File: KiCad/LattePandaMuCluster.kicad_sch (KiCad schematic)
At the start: 0 parts

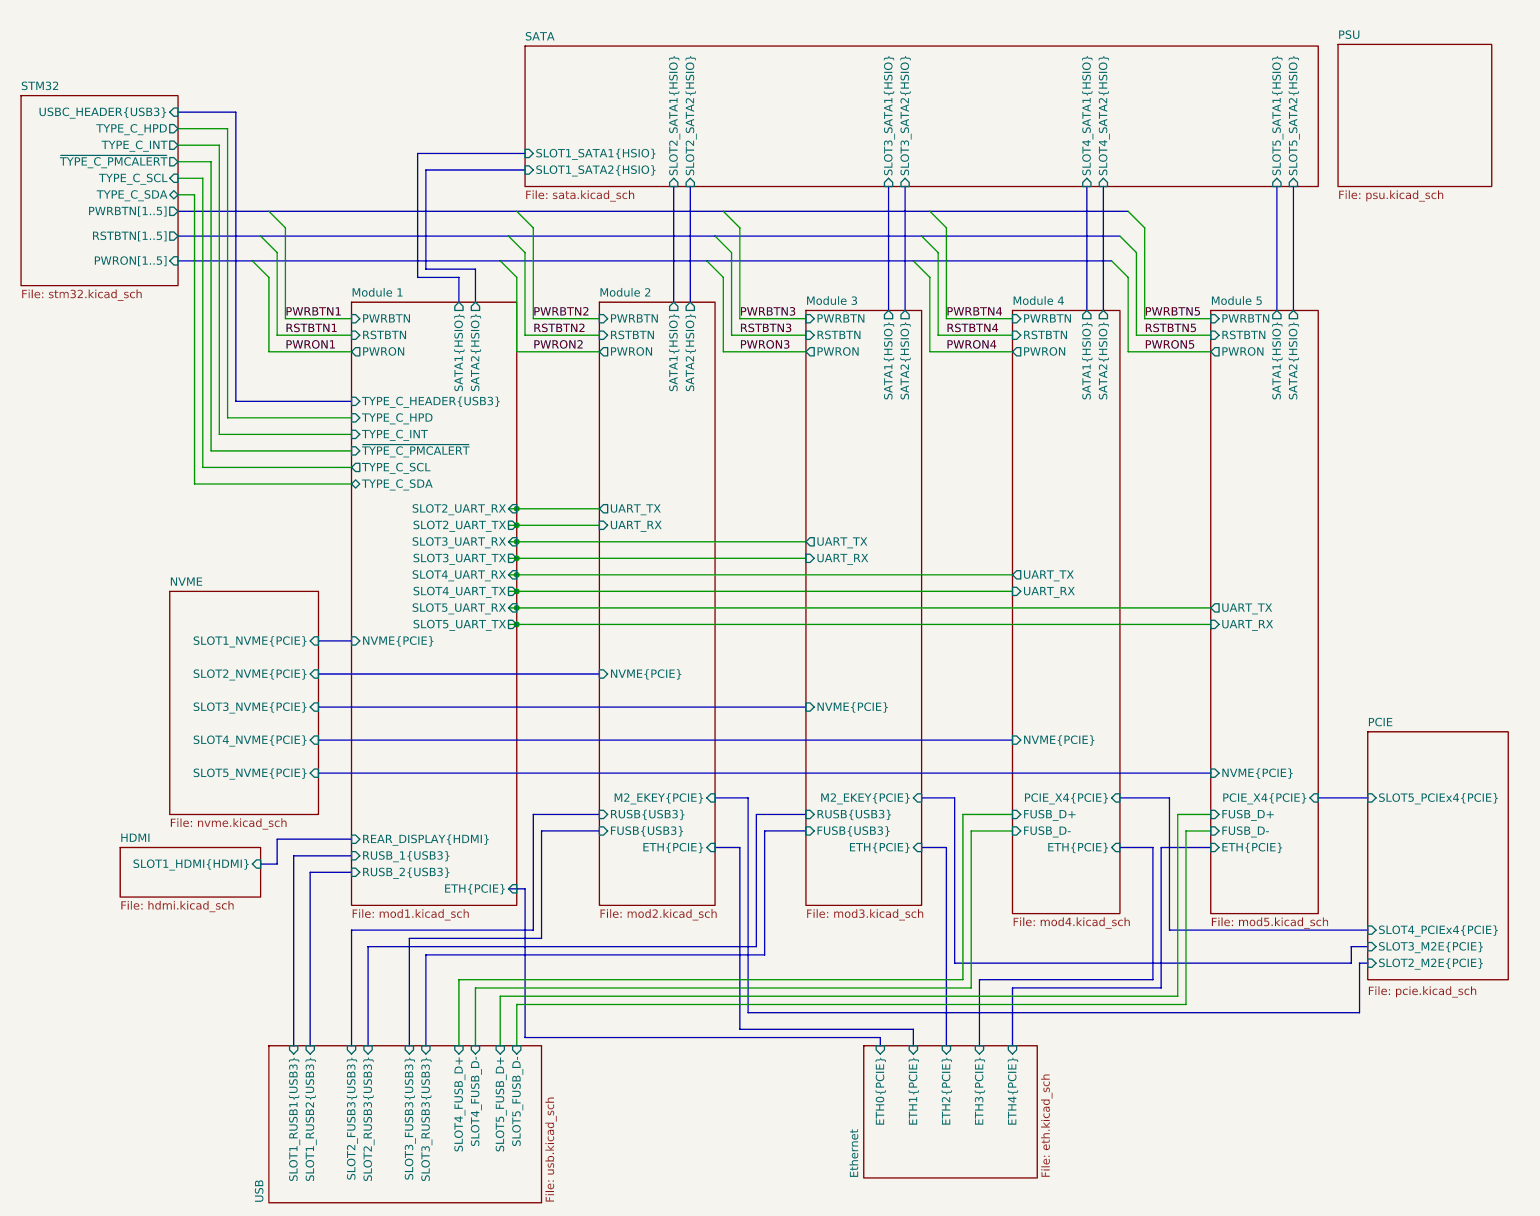
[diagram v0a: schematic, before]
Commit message: Add programming header and power and reset switches
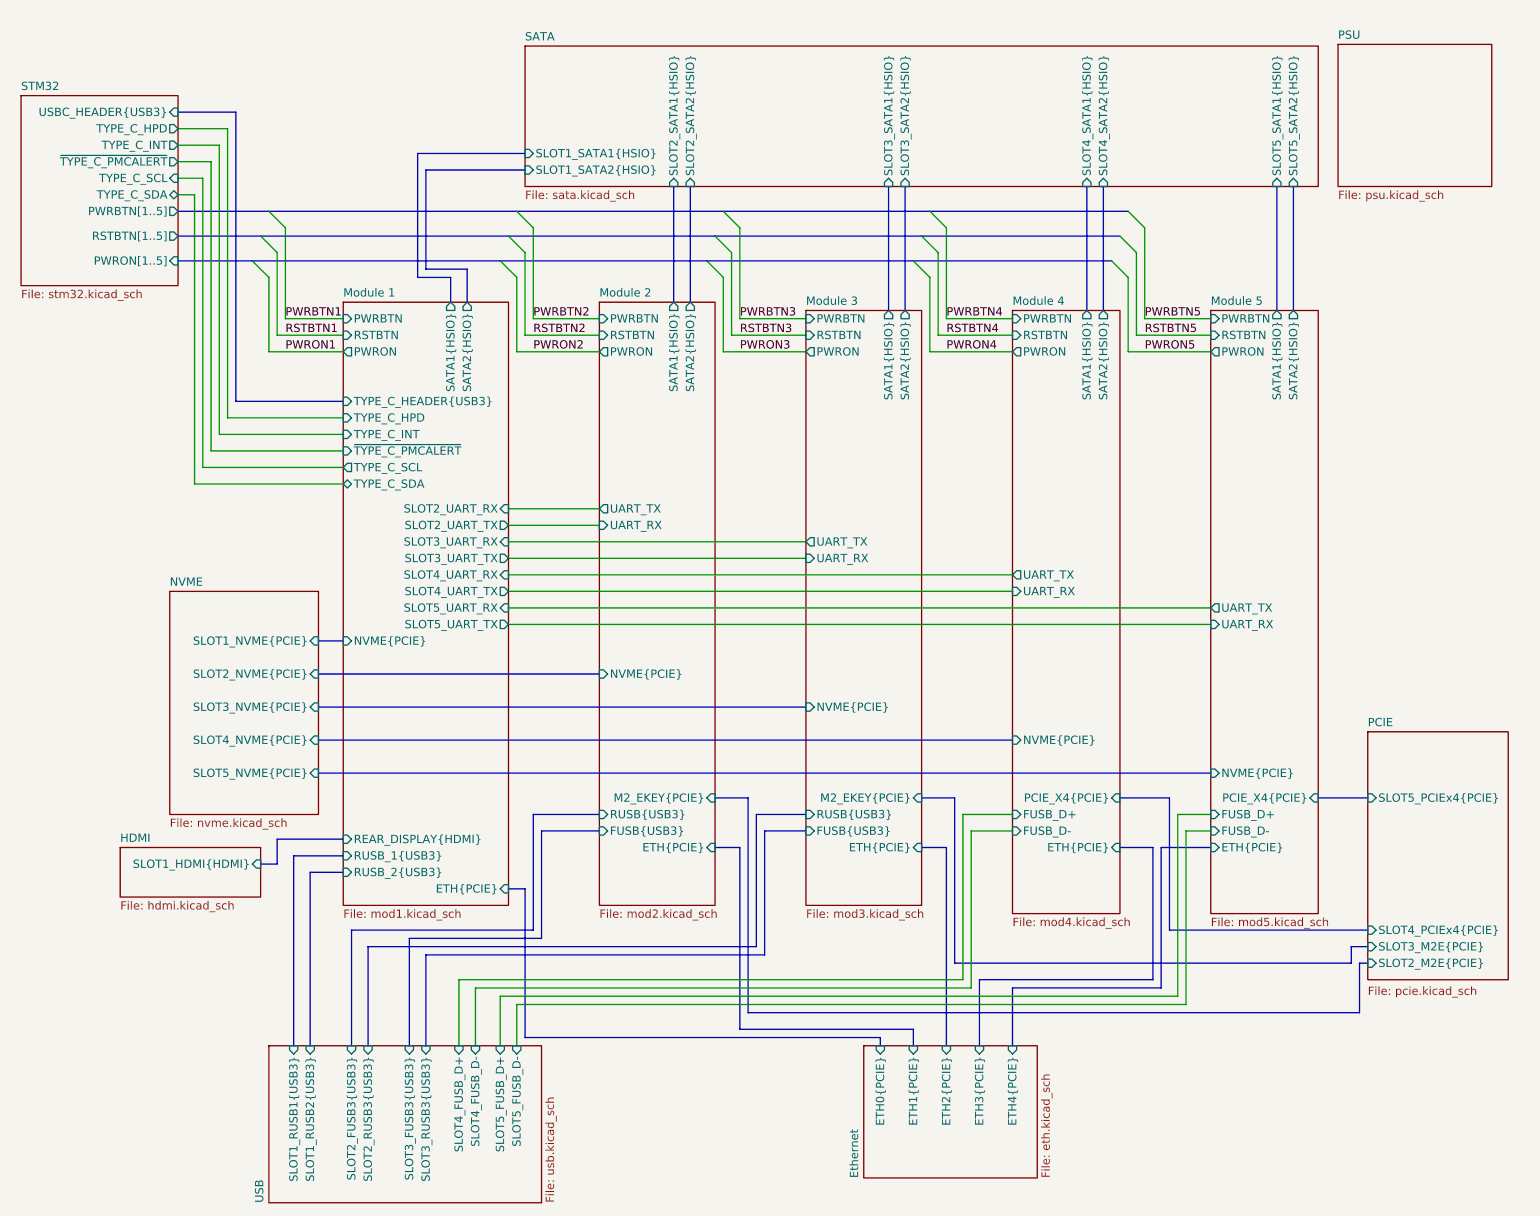
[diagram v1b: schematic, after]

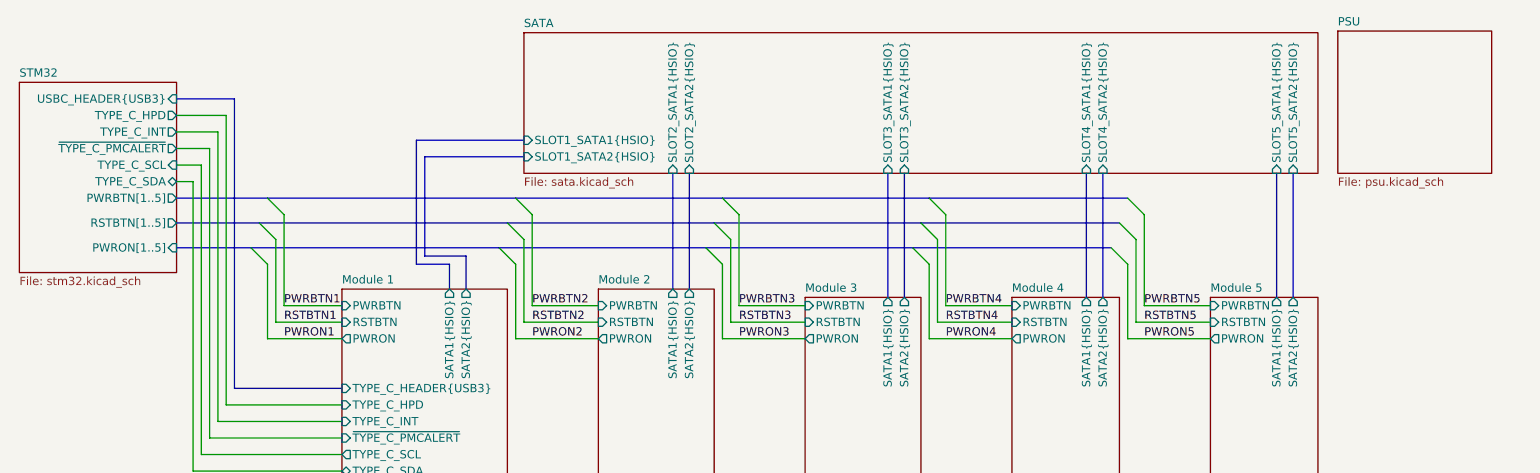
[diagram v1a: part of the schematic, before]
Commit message: Connect PWR_ON and PWR_OK signals
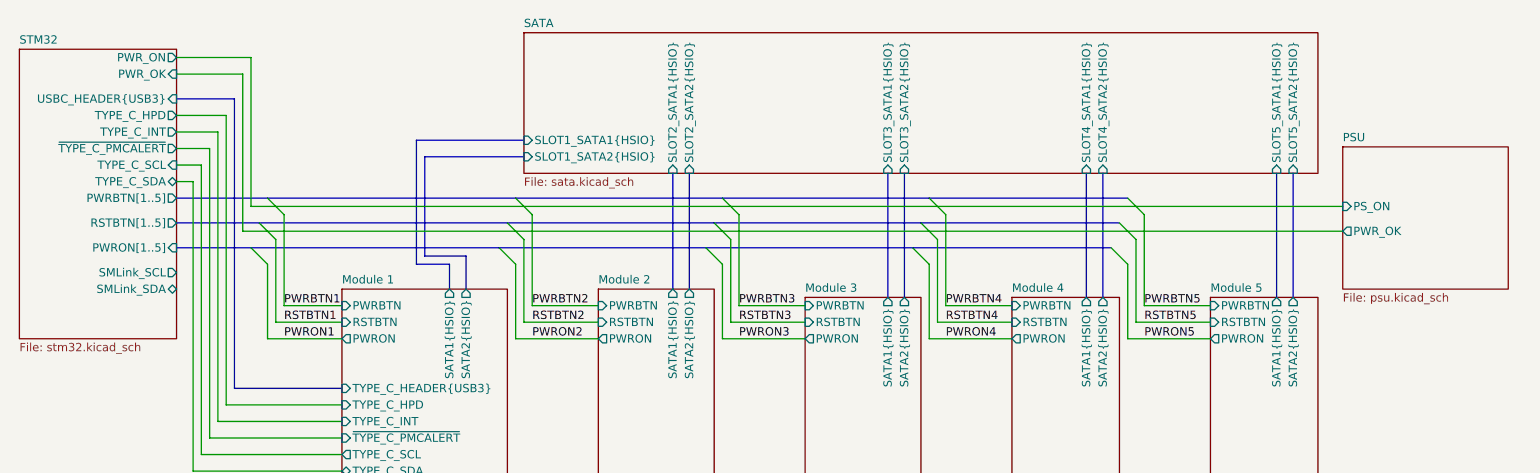
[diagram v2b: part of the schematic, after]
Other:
- sheet PSU ports: added PS_ON, PWR_OK; removed none
- sheet STM32 ports: added PWR_OK, PWR_ON, SMLink_SCL, SMLink_SDA; removed none
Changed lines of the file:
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@@
+	(wire
+		(pts
+			(xy 38.1 21.59) (xy 48.26 21.59)
+		)
+		(stroke
+			(width 0)
+			(type default)
+		)
+	)
 	(wire
 		(pts
@@
 		)
 	)
+	(wire
+		(pts
+			(xy 48.26 21.59) (xy 48.26 45.72)
+		)
+		(stroke
+			(width 0)
+			(type default)
+		)
+	)
 	(bus
 		(pts
@@
 		)
 	)
+	(wire
+		(pts
+			(xy 49.53 41.91) (xy 49.53 19.05)
+		)
+		(stroke
+			(width 0)
+			(type default)
+		)
+	)
 	(bus
 		(pts
@@
 	(wire
 		(pts
+			(xy 48.26 45.72) (xy 217.17 45.72)
+		)
+		(stroke
+			(width 0)
+			(type default)
+		)
+	)
+	(wire
+		(pts
 			(xy 156.21 57.15) (xy 166.37 57.15)
 		)
@@
 	(wire
 		(pts
+			(xy 49.53 19.05) (xy 38.1 19.05)
+		)
+		(stroke
+			(width 0)
+			(type default)
+		)
+	)
+	(wire
+		(pts
 			(xy 63.5 74.93) (xy 44.45 74.93)
 		)
@@
 		(pts
 			(xy 193.04 135.89) (xy 193.04 162.56)
+		)
+		(stroke
+			(width 0)
+			(type default)
+		)
+	)
+	(wire
+		(pts
+			(xy 217.17 41.91) (xy 49.53 41.91)
 		)
 		(stroke
@@
 	)
 	(sheet
-		(at 13.97 22.86)
-		(size 24.13 29.21)
+		(at 13.97 17.78)
+		(size 24.13 44.45)
 		(exclude_from_sim no)
 		(in_bom yes)
@@
 		)
 		(property "Sheetname" "STM32"
-			(at 13.97 22.1484 0)
+			(at 13.97 17.0684 0)
 			(effects
 				(font
@@
 		)
 		(property "Sheetfile" "stm32.kicad_sch"
-			(at 13.97 52.6546 0)
+			(at 13.97 62.8146 0)
 			(effects
 				(font
@@
 		(pin "RSTBTN[1..5]" output
 			(at 38.1 44.45 0)
+			(effects
+				(font
+					(size 1.27 1.27)
+				)
+				(justify right)
+			)
+		)
+		(pin "PWR_OK" input
+			(at 38.1 21.59 0)
+			(effects
+				(font
+					(size 1.27 1.27)
+				)
+				(justify right)
+			)
+		)
+		(pin "PWR_ON" output
+			(at 38.1 19.05 0)
+			(effects
+				(font
+					(size 1.27 1.27)
+				)
+				(justify right)
+			)
+		)
+		(pin "SMLink_SCL" output
+			(at 38.1 52.07 0)
+			(effects
+				(font
+					(size 1.27 1.27)
+				)
+				(justify right)
+			)
+		)
+		(pin "SMLink_SDA" bidirectional
+			(at 38.1 54.61 0)
 			(effects
 				(font
@@
 	)
 	(sheet
-		(at 216.408 14.986)
-		(size 23.622 21.844)
+		(at 217.17 32.766)
+		(size 25.4 21.844)
 		(exclude_from_sim no)
 		(in_bom yes)
@@
 		)
 		(property "Sheetname" "PSU"
-			(at 216.408 14.2744 0)
+			(at 217.17 32.0544 0)
 			(effects
 				(font
@@
 		)
 		(property "Sheetfile" "psu.kicad_sch"
-			(at 216.408 37.4146 0)
+			(at 217.17 55.1946 0)
 			(effects
 				(font
@@
 			)
 		)
+		(pin "PS_ON" input
+			(at 217.17 41.91 180)
+			(effects
+				(font
+					(size 1.27 1.27)
+				)
+				(justify left)
+			)
+		)
+		(pin "PWR_OK" output
+			(at 217.17 45.72 180)
+			(effects
+				(font
+					(size 1.27 1.27)
+				)
+				(justify left)
+			)
+		)

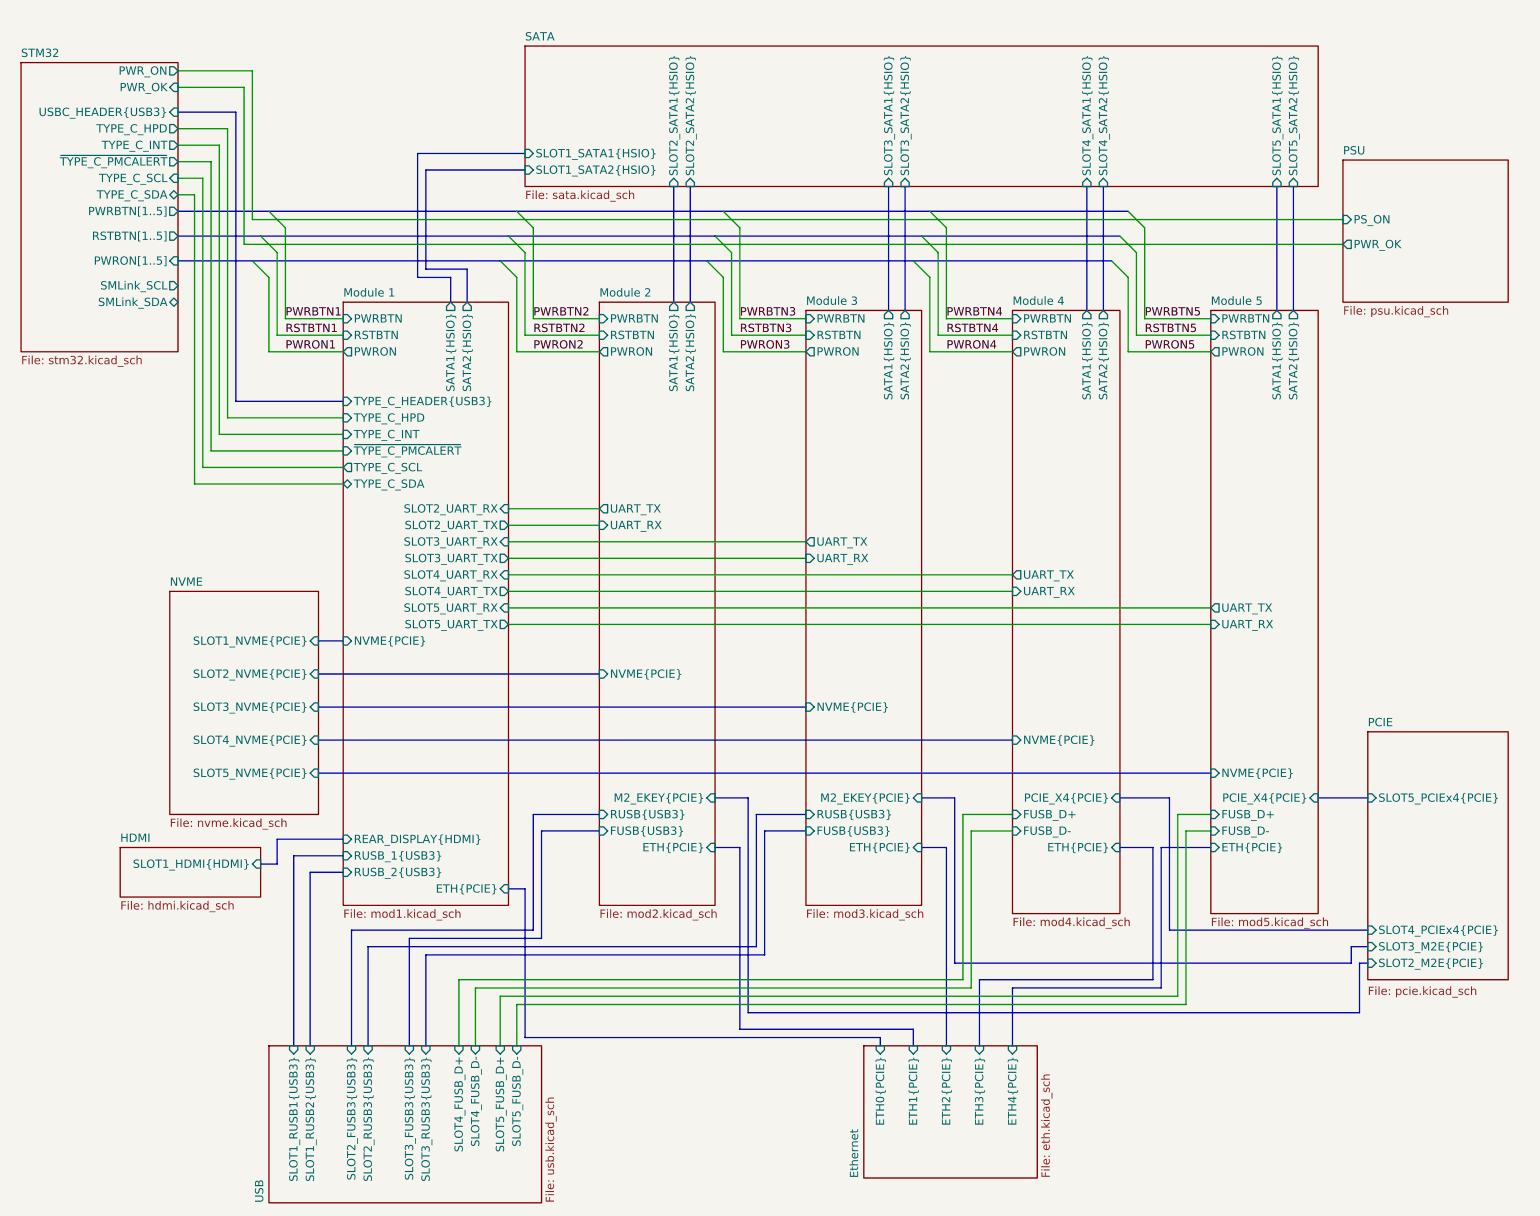
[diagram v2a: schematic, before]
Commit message: Add TPS65987D PD controller, switch stm32 to cheaper one
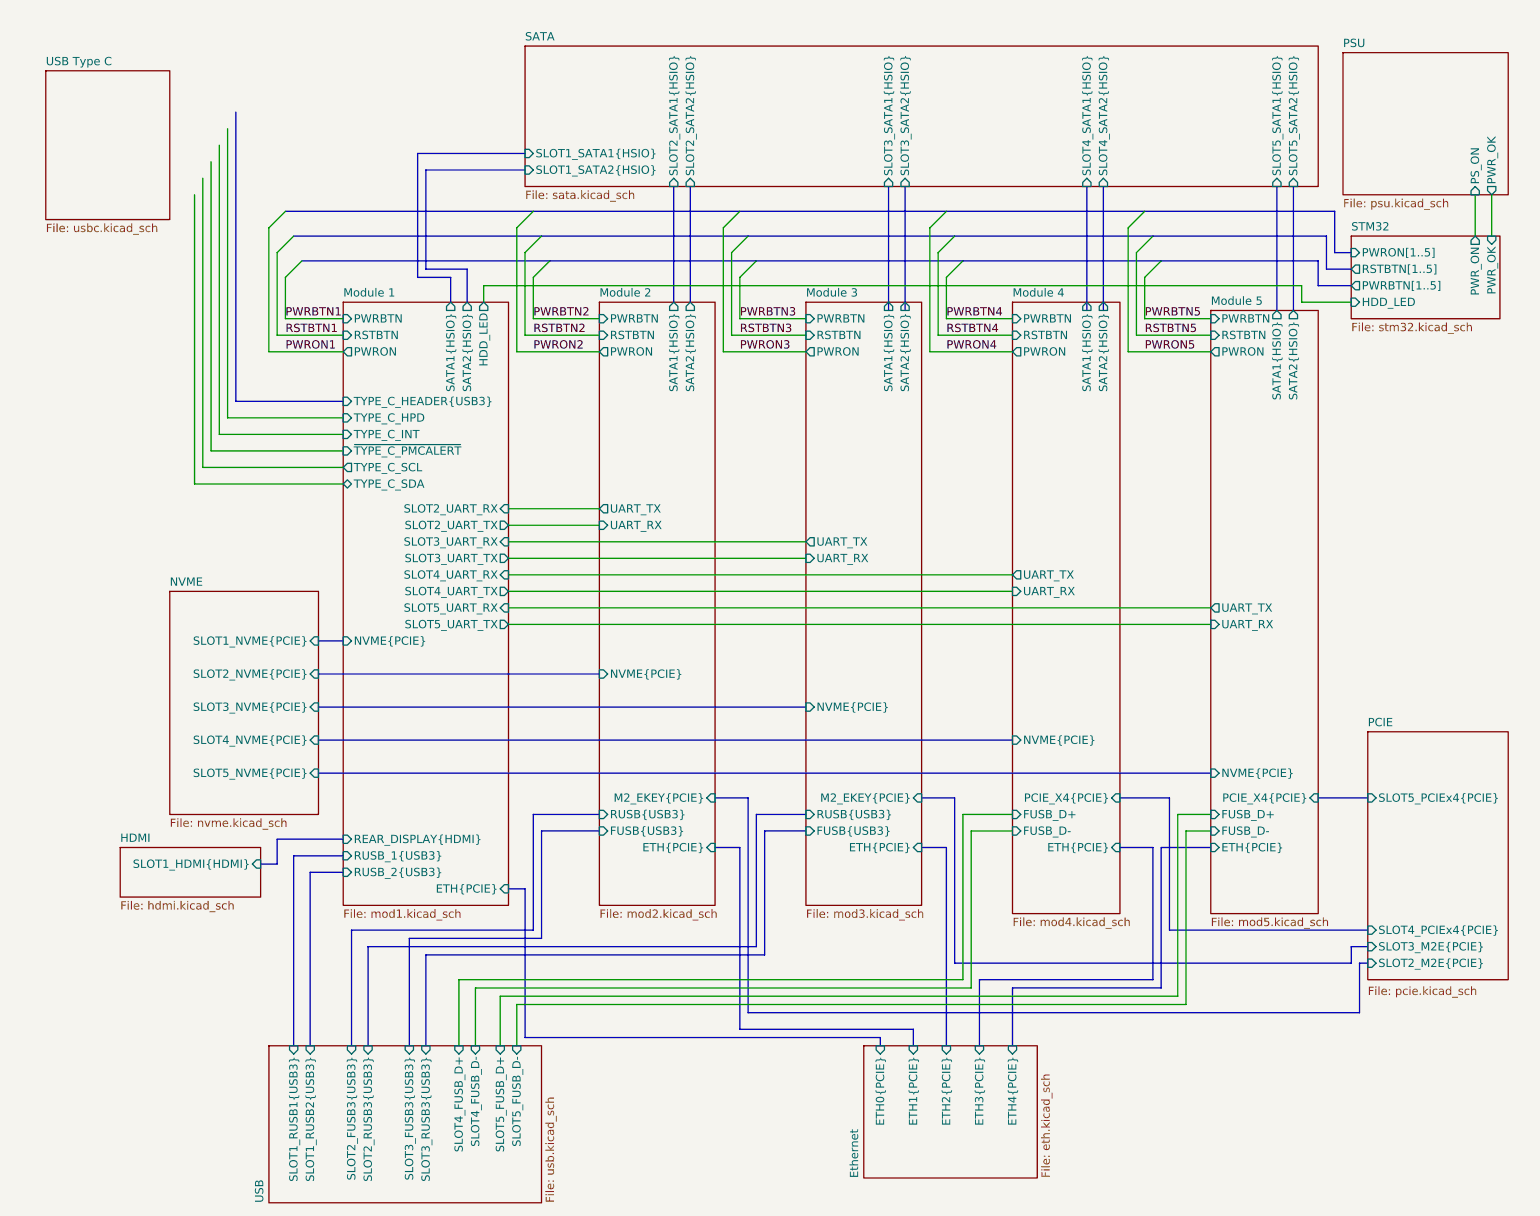
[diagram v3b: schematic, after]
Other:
- added sheet USB Type C (usbc.kicad_sch)
- sheet Module 1 ports: added HDD_LED; removed none
- sheet STM32 ports: added HDD_LED; removed SMLink_SCL, SMLink_SDA, TYPE_C_HPD, TYPE_C_INT, TYPE_C_SCL, TYPE_C_SDA, USBC_HEADER{USB3}, ~{TYPE_C_PMCALERT}
